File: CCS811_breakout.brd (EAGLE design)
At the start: 18.4 x 12.4 mm, 4 parts, among them U10 CCS811

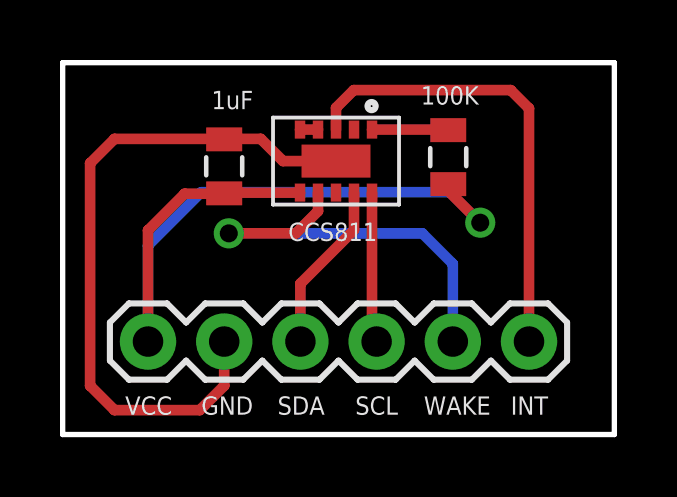
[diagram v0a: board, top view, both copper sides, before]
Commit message: Optimized layout; reduced board size
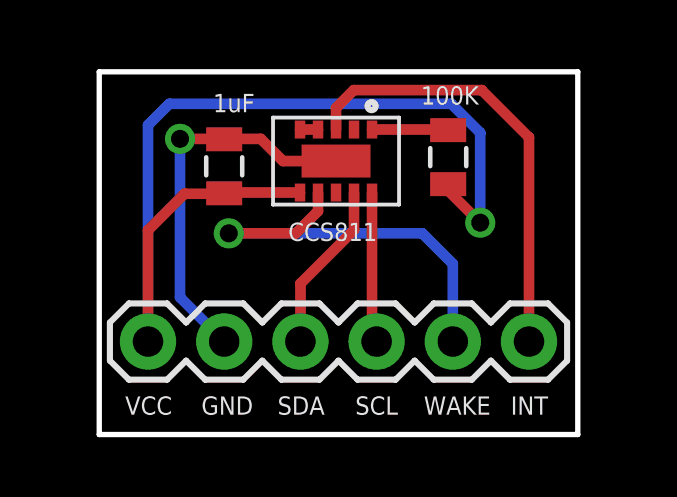
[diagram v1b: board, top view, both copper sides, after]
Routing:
- net GND: track 22.9 -> 12.9 mm, vias 0 -> 1
- net VCC: track 26.5 -> 33.0 mm
- net INT: track 15.4 -> 14.9 mm
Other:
- board size 18.4 x 12.4 mm -> 16 x 12.1 mm
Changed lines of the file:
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@@
 <board>
 <plain>
-<wire x1="0.2032" y1="-0.4064" x2="18.5928" y2="-0.4064" width="0.1778" layer="20"/>
-<wire x1="18.5928" y1="-0.4064" x2="18.5928" y2="11.9888" width="0.1778" layer="20"/>
-<wire x1="18.5928" y1="11.9888" x2="0.2032" y2="11.9888" width="0.1778" layer="20"/>
-<wire x1="0.2032" y1="11.9888" x2="0.2032" y2="-0.4064" width="0.1778" layer="20"/>
+<wire x1="1.4224" y1="-0.4064" x2="17.3736" y2="-0.4064" width="0.1778" layer="20"/>
+<wire x1="17.3736" y1="-0.4064" x2="17.3736" y2="11.684" width="0.1778" layer="20"/>
+<wire x1="17.3736" y1="11.684" x2="1.4224" y2="11.684" width="0.1778" layer="20"/>
+<wire x1="1.4224" y1="11.684" x2="1.4224" y2="-0.4064" width="0.1778" layer="20"/>
 <text x="2.286" y="0.254" size="0.6096" layer="121" font="vector">VCC</text>
 <text x="4.826" y="0.254" size="0.6096" layer="121" font="vector">GND</text>
@@
 <attribute name="MPN" value="" x="5.588" y="8.5344" size="1.778" layer="27" rot="R90" display="off"/>
 <attribute name="MF" value="" x="5.588" y="8.5344" size="1.778" layer="27" rot="R90" display="off"/>
-<attribute name="VALUE" x="6.5532" y="11.049" size="0.6096" layer="121" font="vector" rot="R180"/>
+<attribute name="VALUE" x="6.604" y="10.9474" size="0.6096" layer="121" font="vector" rot="R180"/>
 </element>
 <element name="R2" library="SparkFun-Passives" package="0805" value="100K" x="13.0556" y="8.8392" smashed="yes" rot="R270">
@@
 <wire x1="6.8072" y1="9.4488" x2="5.6024" y2="9.4488" width="0.3556" layer="1"/>
 <wire x1="5.6024" y1="9.4488" x2="5.588" y2="9.4344" width="0.4064" layer="1"/>
-<wire x1="5.588" y1="2.6924" x2="5.588" y2="1.2192" width="0.3556" layer="1"/>
-<wire x1="5.588" y1="1.2192" x2="4.7752" y2="0.4064" width="0.3556" layer="1"/>
-<wire x1="1.9304" y1="9.4488" x2="5.5736" y2="9.4488" width="0.3556" layer="1"/>
 <wire x1="5.5736" y1="9.4488" x2="5.588" y2="9.4344" width="0.4064" layer="1"/>
-<wire x1="1.9304" y1="9.4488" x2="1.1176" y2="8.636" width="0.3556" layer="1"/>
-<wire x1="1.1176" y1="8.636" x2="1.1176" y2="1.2192" width="0.3556" layer="1"/>
-<wire x1="1.1176" y1="1.2192" x2="1.9304" y2="0.4064" width="0.3556" layer="1"/>
-<wire x1="1.9304" y1="0.4064" x2="4.7752" y2="0.4064" width="0.3556" layer="1"/>
+<wire x1="5.5736" y1="9.4488" x2="4.1148" y2="9.4488" width="0.3556" layer="1"/>
+<via x="4.1148" y="9.4488" extent="1-16" drill="0.6"/>
+<wire x1="4.1148" y1="9.4488" x2="4.1148" y2="4.1656" width="0.3556" layer="16"/>
+<wire x1="4.1148" y1="4.1656" x2="5.588" y2="2.6924" width="0.3556" layer="16"/>
 </signal>
 <signal name="VCC">
@@
 <wire x1="13.0556" y1="7.7216" x2="14.1224" y2="6.6548" width="0.3556" layer="1"/>
 <via x="14.1224" y="6.6548" extent="1-16" drill="0.6"/>
-<wire x1="14.1224" y1="6.6548" x2="13.1064" y2="7.6708" width="0.3556" layer="16"/>
-<wire x1="13.1064" y1="7.6708" x2="4.826" y2="7.6708" width="0.3556" layer="16"/>
-<wire x1="4.826" y1="7.6708" x2="3.048" y2="5.8928" width="0.3556" layer="16"/>
-<wire x1="3.048" y1="5.8928" x2="3.048" y2="2.6924" width="0.3556" layer="16"/>
+<wire x1="14.1224" y1="6.6548" x2="14.1224" y2="9.652" width="0.3556" layer="16"/>
+<wire x1="14.1224" y1="9.652" x2="13.1572" y2="10.6172" width="0.3556" layer="16"/>
+<wire x1="13.1572" y1="10.6172" x2="3.7592" y2="10.6172" width="0.3556" layer="16"/>
+<wire x1="3.7592" y1="10.6172" x2="3.048" y2="9.906" width="0.3556" layer="16"/>
+<wire x1="3.048" y1="9.906" x2="3.048" y2="2.6924" width="0.3556" layer="16"/>
 </signal>
 <signal name="SCL">
@@
 <wire x1="9.3152" y1="9.7584" x2="9.3152" y2="10.4836" width="0.3556" layer="1"/>
 <wire x1="9.3152" y1="10.4836" x2="9.906" y2="11.0744" width="0.3556" layer="1"/>
-<wire x1="9.906" y1="11.0744" x2="15.1384" y2="11.0744" width="0.3556" layer="1"/>
-<wire x1="15.1384" y1="11.0744" x2="15.748" y2="10.4648" width="0.3556" layer="1"/>
-<wire x1="15.748" y1="10.4648" x2="15.748" y2="2.6924" width="0.3556" layer="1"/>
+<wire x1="9.906" y1="11.0744" x2="14.1732" y2="11.0744" width="0.3556" layer="1"/>
+<wire x1="14.1732" y1="11.0744" x2="15.748" y2="9.4996" width="0.3556" layer="1"/>
+<wire x1="15.748" y1="9.4996" x2="15.748" y2="2.6924" width="0.3556" layer="1"/>
 </signal>
 <signal name="N$2">
 <contactref element="U10" pad="5"/>
 <contactref element="U10" pad="4"/>
-<wire x1="8.7152" y1="9.7584" x2="8.1152" y2="9.7584" width="0.3556" layer="1"/>
+<wire x1="8.1152" y1="9.7584" x2="8.7152" y2="9.7584" width="0.3556" layer="1"/>
 </signal>
 </signals>
